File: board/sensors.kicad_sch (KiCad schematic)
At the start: 25 parts, among them U6 MAX-M8C

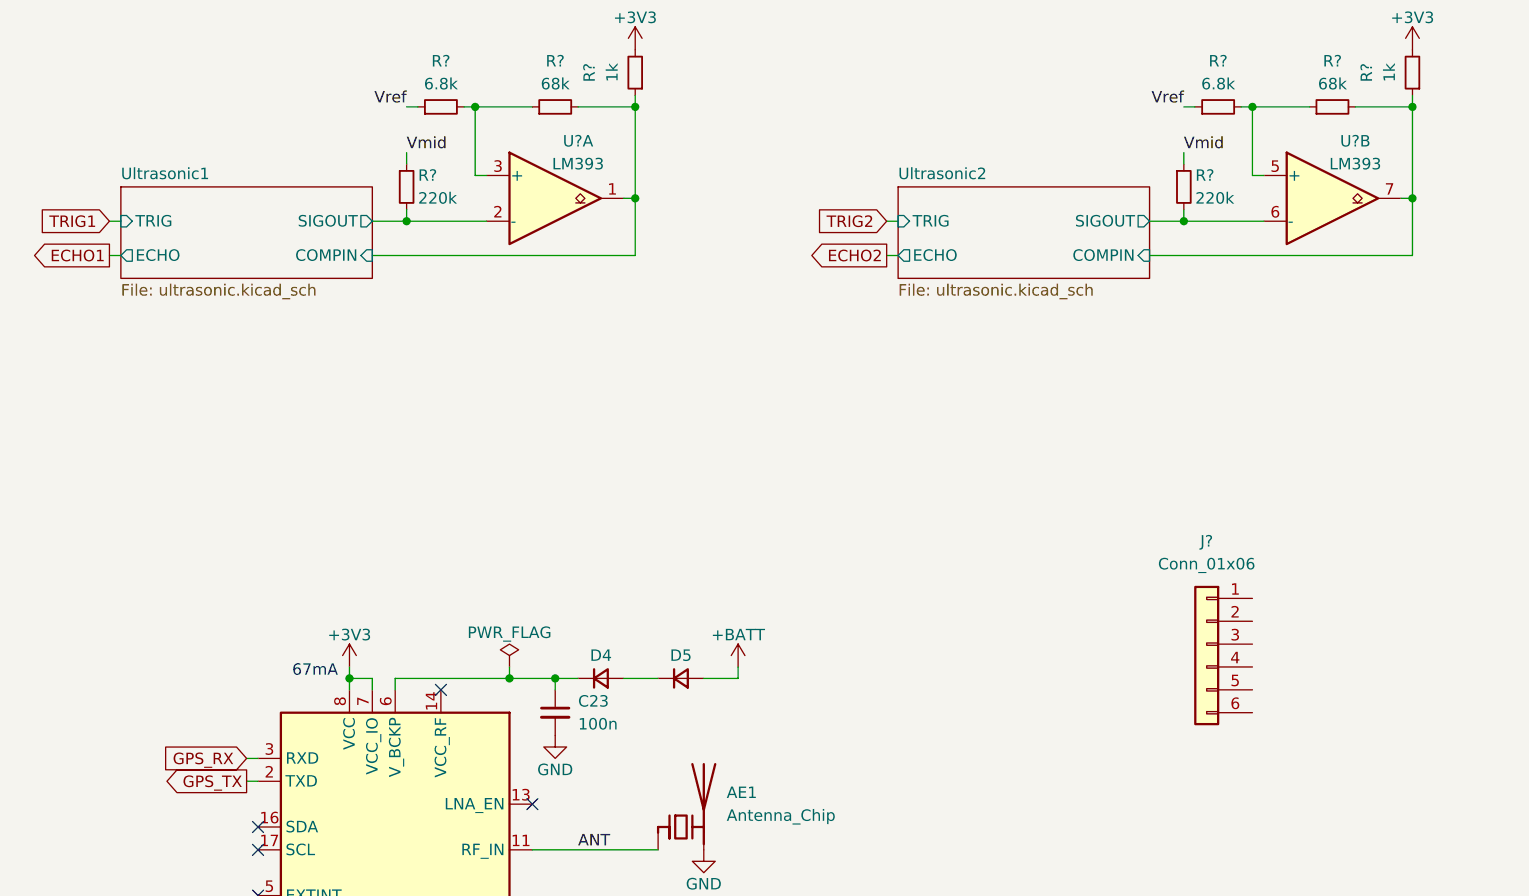
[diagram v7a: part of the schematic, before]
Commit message: Replaced the component groups to get a tighter fit and routed most of the ultrasonic sensors
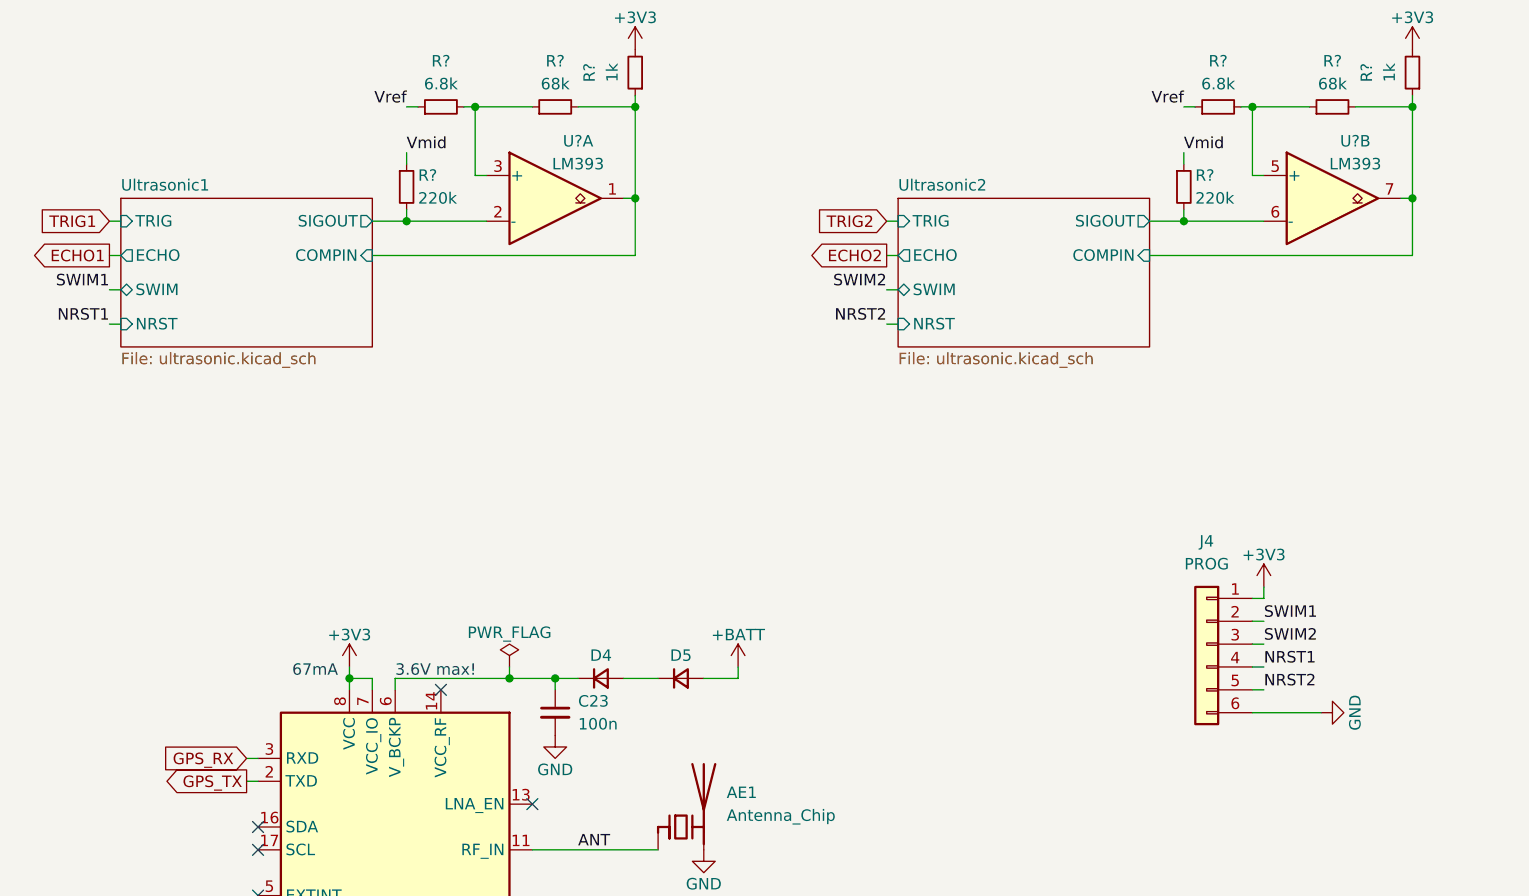
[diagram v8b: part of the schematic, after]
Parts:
- D4, D5: footprint Diode_SMD:D_SMA -> Diode_SMD:D_SOD-123F; JLC_PN C2480 -> C64898; MPN SS14 -> SM4007PL
- J4: renamed from J?; value Conn_01x06 -> PROG; footprint (none) -> Connector_PinHeader_2.54mm:PinHeader_1x06_P2.54mm_Horizontal; JLC_BasicPart (none) -> no; JLC_PN (none) -> C492414; MPN (none) -> PZ254R-11-06P; Manufacturer (none) -> XFCN
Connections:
- net +3V3: now also J4.1 (Pin_1)
- net GND: now also J4.6 (Pin_6)
- net SWIM1: now reaches J4.2 (Pin_2)
- net SWIM2: now reaches J4.3 (Pin_3)
- net NRST1: now reaches J4.4 (Pin_4)
- net NRST2: now reaches J4.5 (Pin_5)
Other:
- sheet Ultrasonic1 ports: added NRST, SWIM; removed none
- sheet Ultrasonic2 ports: added NRST, SWIM; removed none
- note added: "3.6V max!"
